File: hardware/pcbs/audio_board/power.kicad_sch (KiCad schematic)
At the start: 30 parts, among them Q1 S8050, U2 LP5907MFX-3.3, U3 LM5158

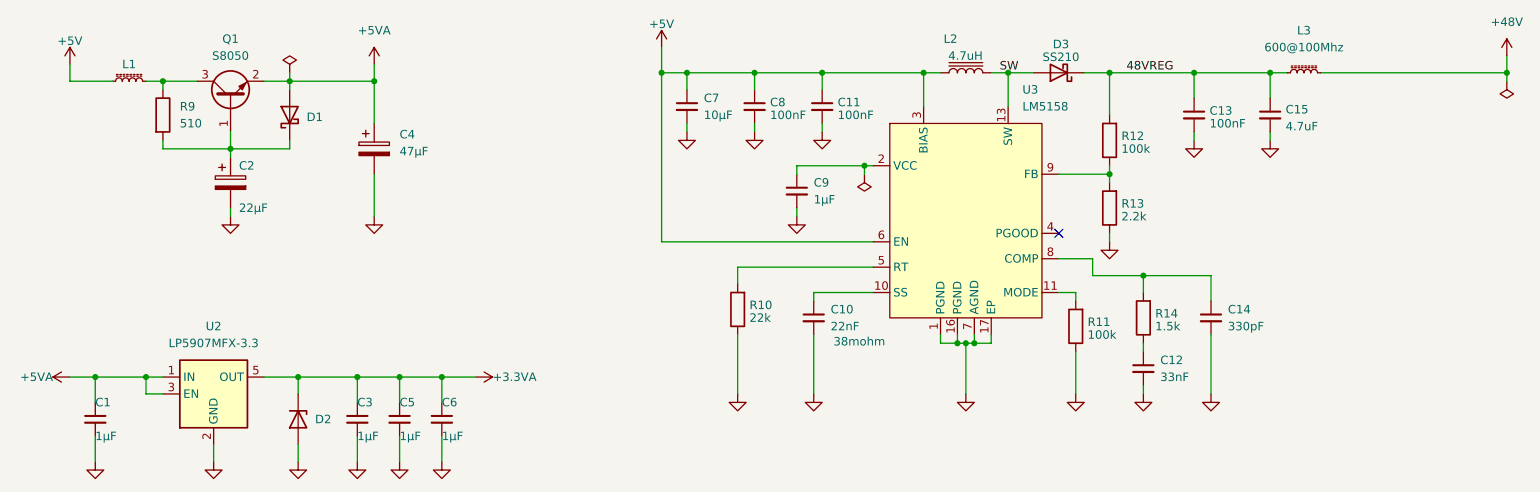
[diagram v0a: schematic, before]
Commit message: revise BOM
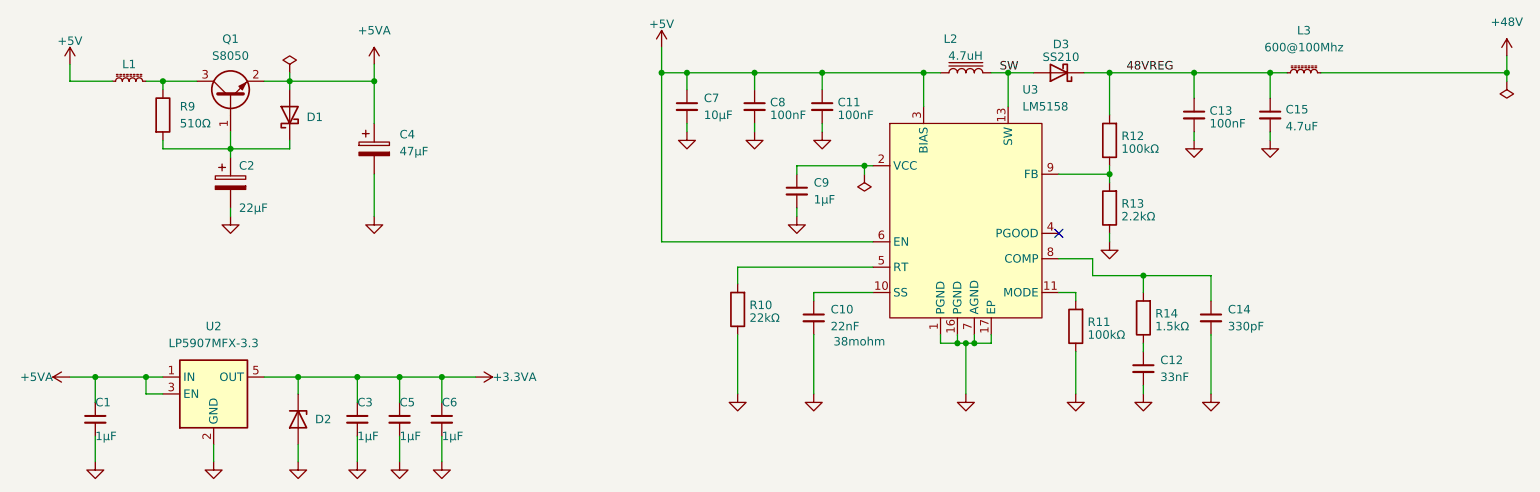
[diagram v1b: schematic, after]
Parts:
- C15: MPN (none) -> C 4.7μF 16V 0805
- L1, L3: MPN (none) -> BLM21AG601SN1D
- Q1: MPN (none) -> BC817-40
- R10: value 22k -> 22kΩ; MPN (none) -> R 22kΩ 125mW 1% 0805
- R11, R12: value 100k -> 100kΩ; MPN (none) -> R 100kΩ 125mW 1% 0805
- R13: value 2.2k -> 2.2kΩ; MPN (none) -> R 2.2kΩ 125mW 1% 0805
- R14: value 1.5k -> 1.5kΩ; MPN (none) -> R 1.5kΩ 125mW 1% 0805
- R9: value 510 -> 510Ω; MPN (none) -> R 510Ω 125mW 1% 0805
- U3: MPN (none) -> LM5158QRTERQ1
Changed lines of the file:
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@@
+			)
+		)
+		(property "MPN" "BLM21AG601SN1D"
+			(at 54.61 63.5 90)
+			(effects
+				(font
+					(size 1.27 1.27)
+				)
+				(hide yes)
 			)
 		)
@@
 			)
 		)
-		(property "Value" "22k"
+		(property "Value" "22kΩ"
 			(at 147.828 99.0673 0)
 			(effects
@@
 		)
 		(property "Description" ""
+			(at 146.05 97.79 0)
+			(effects
+				(font
+					(size 1.27 1.27)
+				)
+				(hide yes)
+			)
+		)
+		(property "MPN" "R 22kΩ 125mW 1% 0805"
 			(at 146.05 97.79 0)
 			(effects
@@
 			)
 		)
+		(property "MPN" "BLM21AG601SN1D"
+			(at 231.14 62.23 90)
+			(effects
+				(font
+					(size 1.27 1.27)
+				)
+				(hide yes)
+			)
+		)
 		(pin "1"
 		)
@@
 			)
 		)
+		(property "MPN" "LM5158QRTERQ1"
+			(at 168.91 67.31 0)
+			(effects
+				(font
+					(size 1.27 1.27)
+				)
+				(hide yes)
+			)
+		)
 		(pin "14"
 		)
@@
 			)
 		)
-		(property "Value" "100k"
+		(property "Value" "100kΩ"
 			(at 198.628 101.6073 0)
 			(effects
@@
 		)
 		(property "Description" ""
+			(at 196.85 100.33 0)
+			(effects
+				(font
+					(size 1.27 1.27)
+				)
+				(hide yes)
+			)
+		)
+		(property "MPN" "R 100kΩ 125mW 1% 0805"
 			(at 196.85 100.33 0)
 			(effects
@@
 			)
 		)
-		(property "Value" "1.5k"
+		(property "Value" "1.5kΩ"
 			(at 208.788 100.3373 0)
 			(effects
@@
 			)
 		)
+		(property "MPN" "R 1.5kΩ 125mW 1% 0805"
+			(at 207.01 99.06 0)
+			(effects
+				(font
+					(size 1.27 1.27)
+				)
+				(hide yes)
+			)
+		)
 		(pin "1"
 		)
@@
 			)
 		)
-		(property "Value" "2.2k"
+		(property "Value" "2.2kΩ"
 			(at 203.708 83.8273 0)
 			(effects
@@
 		)
 		(property "Description" ""
+			(at 201.93 82.55 0)
+			(effects
+				(font
+					(size 1.27 1.27)
+				)
+				(hide yes)
+			)
+		)
+		(property "MPN" "R 2.2kΩ 125mW 1% 0805"
 			(at 201.93 82.55 0)
 			(effects
@@
 			)
 		)
+		(property "MPN" "C 4.7μF 16V 0805"
+			(at 226.06 68.58 0)
+			(effects
+				(font
+					(size 1.27 1.27)
+				)
+				(hide yes)
+			)
+		)
 		(pin "1"
 		)
@@
 			)
 		)
-		(property "Value" "100k"
+		(property "Value" "100kΩ"
 			(at 203.708 73.6673 0)
 			(effects
@@
 		)
 		(property "Description" ""
+			(at 201.93 72.39 0)
+			(effects
+				(font
+					(size 1.27 1.27)
+				)
+				(hide yes)
+			)
+		)
+		(property "MPN" "R 100kΩ 125mW 1% 0805"
 			(at 201.93 72.39 0)
 			(effects
@@
 			)
 		)
+		(property "MPN" "BC817-40"
+			(at 69.85 66.04 90)
+			(effects
+				(font
+					(size 1.27 1.27)
+				)
+				(hide yes)
+			)
+		)
 		(pin "2"
 		)
@@
 			)
 		)
-		(property "Value" "510"
+		(property "Value" "510Ω"
 			(at 62.23 69.8499 0)
 			(effects
@@
 			(at 59.69 68.58 0)
 			(effects
+				(font
+					(size 1.27 1.27)
+				)
+				(hide yes)
+			)
+		)
+		(property "MPN" "R 510Ω 125mW 1% 0805"
+			(at 59.69 68.58 0)
+			(effects

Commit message: slew rate limiting resistors
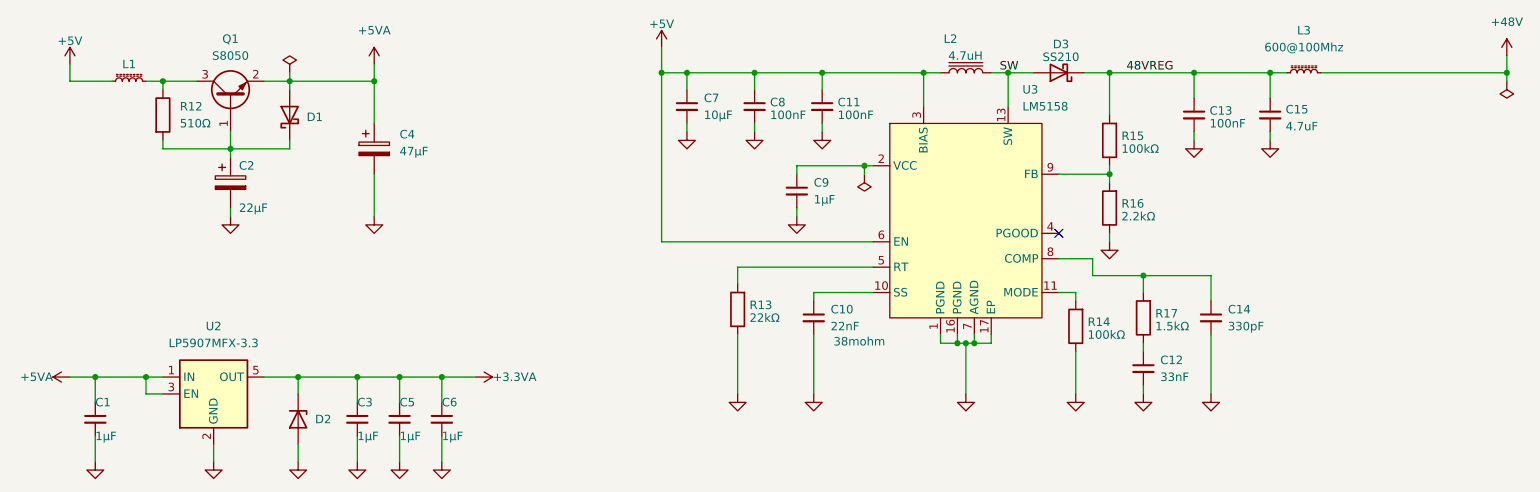
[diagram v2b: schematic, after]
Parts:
- renumbered R9 to R12, R10 to R13, R11 to R14, R12 to R15, R13 to R16, R14 to R17
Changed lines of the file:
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@@
 		(on_board yes)
 		(dnp no)
-		(property "Reference" "R10"
+		(property "Reference" "R13"
 			(at 147.828 97.1463 0)
 			(effects
@@
 			(project "audio_board"
 				(path "/54443f96-c7c5-4432-b890-45b14a1547a1/23b45e70-9f0d-43c3-ad82-81d9481de3a2"
-					(reference "R10")
+					(reference "R13")
 					(unit 1)
 				)
@@
 		(on_board yes)
 		(dnp no)
-		(property "Reference" "R11"
+		(property "Reference" "R14"
 			(at 198.628 99.6863 0)
 			(effects
@@
 			(project "audio_board"
 				(path "/54443f96-c7c5-4432-b890-45b14a1547a1/23b45e70-9f0d-43c3-ad82-81d9481de3a2"
-					(reference "R11")
+					(reference "R14")
 					(unit 1)
 				)
@@
 		(on_board yes)
 		(dnp no)
-		(property "Reference" "R14"
+		(property "Reference" "R17"
 			(at 208.788 98.4163 0)
 			(effects
@@
 			(project "audio_board"
 				(path "/54443f96-c7c5-4432-b890-45b14a1547a1/23b45e70-9f0d-43c3-ad82-81d9481de3a2"
-					(reference "R14")
+					(reference "R17")
 					(unit 1)
 				)
@@
 		(on_board yes)
 		(dnp no)
-		(property "Reference" "R13"
+		(property "Reference" "R16"
 			(at 203.708 81.9063 0)
 			(effects
@@
 			(project "audio_board"
 				(path "/54443f96-c7c5-4432-b890-45b14a1547a1/23b45e70-9f0d-43c3-ad82-81d9481de3a2"
-					(reference "R13")
+					(reference "R16")
 					(unit 1)
 				)
@@
 		(on_board yes)
 		(dnp no)
-		(property "Reference" "R12"
+		(property "Reference" "R15"
 			(at 203.708 71.7463 0)
 			(effects
@@
 			(project "audio_board"
 				(path "/54443f96-c7c5-4432-b890-45b14a1547a1/23b45e70-9f0d-43c3-ad82-81d9481de3a2"
-					(reference "R12")
+					(reference "R15")
 					(unit 1)
 				)
@@
 		(dnp no)
 		(fields_autoplaced yes)
-		(property "Reference" "R9"
+		(property "Reference" "R12"
 			(at 62.23 67.3099 0)
 			(effects
@@
 			(project "audio_board"
 				(path "/54443f96-c7c5-4432-b890-45b14a1547a1/23b45e70-9f0d-43c3-ad82-81d9481de3a2"
-					(reference "R9")
-					(unit 1)
-				)
+					(reference "R12")
+					(unit 1)
+				)

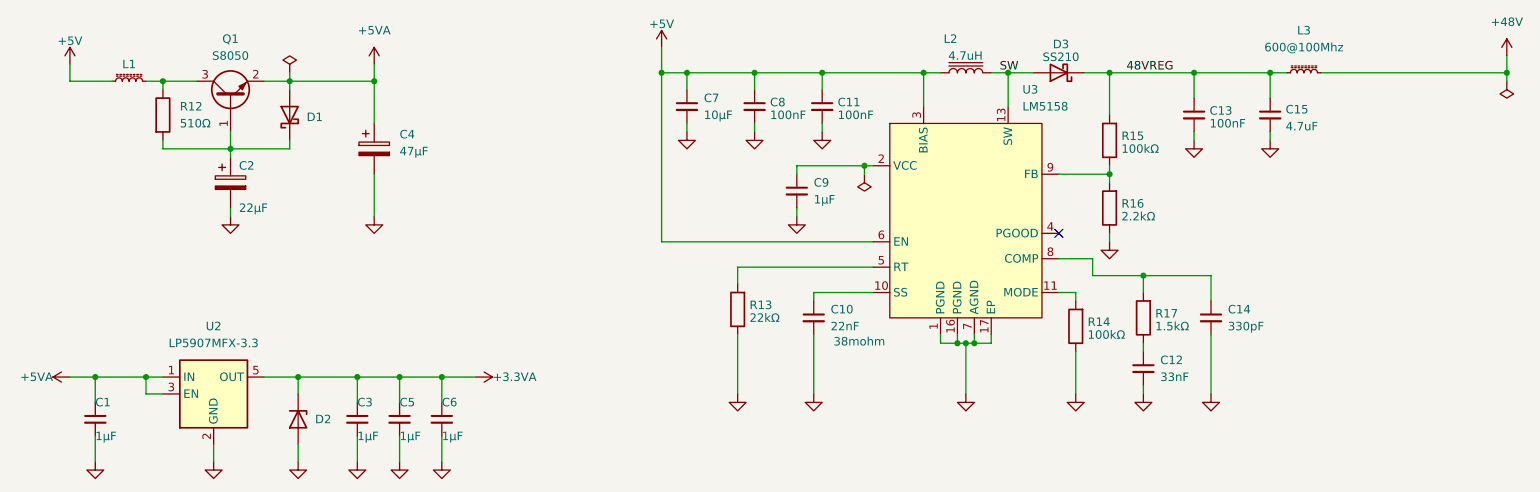
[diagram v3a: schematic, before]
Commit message: fix audioboard phantom power and some labels
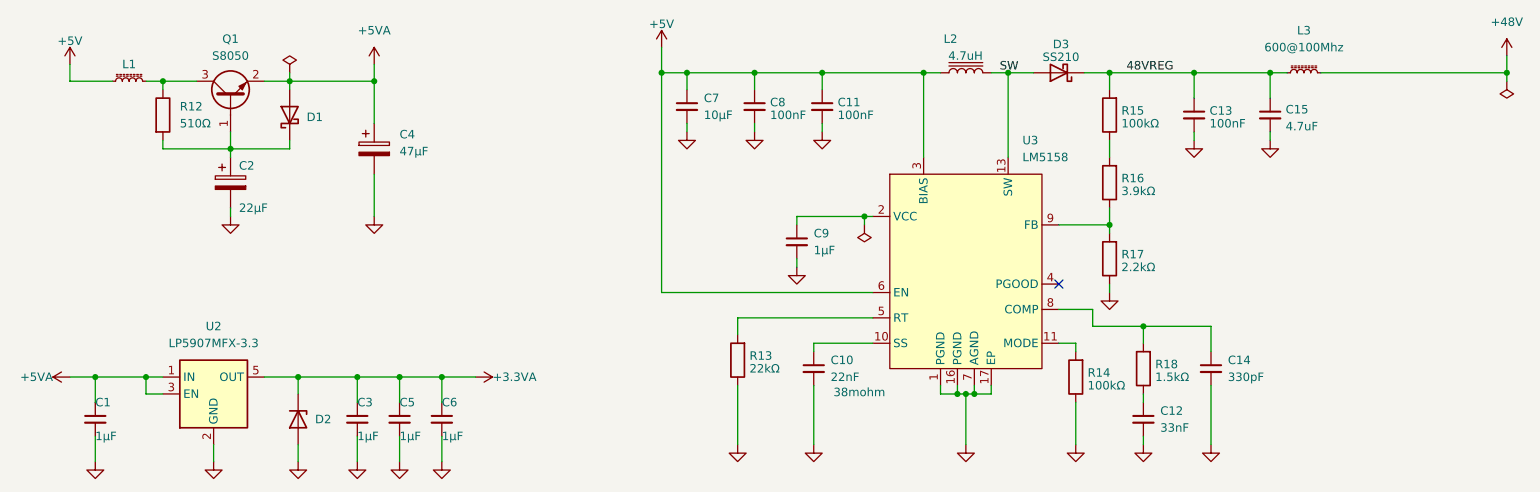
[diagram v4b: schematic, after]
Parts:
- added R16: 3.9kΩ, Resistor_SMD:R_0805_2012Metric, symbol Device:R
- renumbered R16 to R17, R17 to R18
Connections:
- net at R17.2, U3.9 (FB): now also R16.1; no longer R15.1
- new net: R15.1, R16.2
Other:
- moved on the sheet: C10, C12, C14, C9, R13, R14, R15, R17, R18, U3
